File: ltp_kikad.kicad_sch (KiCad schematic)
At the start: 27 parts, among them IC1 SamacSys_Parts_HT16K33-28SOP, IC2 SamacSys_Parts_HT16K33-28SOP, J2 RPi_GPIO, J3 SM04B-SRSS-TB(LF)(SN)

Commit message: Minor fixes
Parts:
- added C11 (x2): 10uF, Capacitor_SMD:C_0603_1608Metric, symbol Device:C_Small
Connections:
- net +5V: now also C11.1, C11.1
- net GND: now also C11.2, C11.2
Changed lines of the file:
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@@
+    (stroke (width 0) (type default))
+  )
+  (wire (pts (xy 194.31 64.77) (xy 194.31 72.39))
     (stroke (width 0) (type default))
   )
@@
   )
   (wire (pts (xy 166.37 60.96) (xy 171.45 60.96))
+    (stroke (width 0) (type default))
+  )
+  (wire (pts (xy 273.05 110.49) (xy 273.05 118.11))
     (stroke (width 0) (type default))
   )
@@
     )
   )
+  (symbol (lib_id "power:GND") (at 273.05 123.19 0) (unit 1)
+    (in_bom yes) (on_board yes) (dnp no)
+    (property "Reference" "#PWR038" (at 273.05 129.54 0)
+      (effects (font (size 1.27 1.27)) hide)
+    )
+    (property "Value" "GND" (at 273.177 127.5842 0)
+      (effects (font (size 1.27 1.27)))
+    )
+    (property "Footprint" "" (at 273.05 123.19 0)
+      (effects (font (size 1.27 1.27)) hide)
+    )
+    (property "Datasheet" "" (at 273.05 123.19 0)
+      (effects (font (size 1.27 1.27)) hide)
+    )
+    (pin "1")
+    (instances
+      (project "LTP305_ESP32_CLOCK"
+        (path "/c007e288-8439-49d9-bbdf-49724c34958c"
+          (reference "#PWR038") (unit 1)
+        )
+      )
+      (project "ltp_kikad"
+        (path "/eed35b77-cbf9-4596-9b17-2558f81058ba"
+          (reference "#PWR028") (unit 1)
+        )
+      )
+    )
+  )
   (symbol (lib_id "power:GND") (at 114.3 137.16 0) (unit 1)
     (in_bom yes) (on_board yes) (dnp no)
@@
         (path "/eed35b77-cbf9-4596-9b17-2558f81058ba"
           (reference "#PWR012") (unit 1)
+        )
+      )
+    )
+  )
+  (symbol (lib_id "Device:C_Small") (at 273.05 120.65 0) (unit 1)
+    (in_bom yes) (on_board yes) (dnp no)
+    (property "Reference" "C11" (at 275.3868 119.4816 0)
+      (effects (font (size 1.27 1.27)) (justify left))
+    )
+    (property "Value" "10uF" (at 267.97 123.19 0)
+      (effects (font (size 1.27 1.27)) (justify left))
+    )
+    (property "Footprint" "Capacitor_SMD:C_0603_1608Metric" (at 273.05 120.65 0)
+      (effects (font (size 1.27 1.27)) hide)
+    )
+    (property "Datasheet" "~" (at 273.05 120.65 0)
+      (effects (font (size 1.27 1.27)) hide)
+    )
+    (pin "1")
+    (pin "2")
+    (instances
+      (project "LTP305_ESP32_CLOCK"
+        (path "/c007e288-8439-49d9-bbdf-49724c34958c"
+          (reference "C11") (unit 1)
+        )
+      )
+      (project "ltp_kikad"
+        (path "/eed35b77-cbf9-4596-9b17-2558f81058ba"
+          (reference "C14") (unit 1)
         )
       )
@@
         (path "/eed35b77-cbf9-4596-9b17-2558f81058ba"
           (reference "DS4") (unit 1)
+        )
+      )
+    )
+  )
+  (symbol (lib_id "power:+5V") (at 273.05 110.49 270) (unit 1)
+    (in_bom yes) (on_board yes) (dnp no)
+    (property "Reference" "#PWR08" (at 269.24 110.49 0)
+      (effects (font (size 1.27 1.27)) hide)
+    )
+    (property "Value" "+5V" (at 277.4442 110.871 0)
+      (effects (font (size 1.27 1.27)))
+    )
+    (property "Footprint" "" (at 273.05 110.49 0)
+      (effects (font (size 1.27 1.27)) hide)
+    )
+    (property "Datasheet" "" (at 273.05 110.49 0)
+      (effects (font (size 1.27 1.27)) hide)
+    )
+    (pin "1")
+    (instances
+      (project "LTP305_ESP32_CLOCK"
+        (path "/c007e288-8439-49d9-bbdf-49724c34958c"
+          (reference "#PWR08") (unit 1)
+        )
+      )
+      (project "ltp_kikad"
+        (path "/eed35b77-cbf9-4596-9b17-2558f81058ba"
+          (reference "#PWR027") (unit 1)
+        )
+      )
+    )
+  )
+  (symbol (lib_id "Device:C_Small") (at 194.31 74.93 0) (unit 1)
+    (in_bom yes) (on_board yes) (dnp no)
+    (property "Reference" "C11" (at 196.6468 73.7616 0)
+      (effects (font (size 1.27 1.27)) (justify left))
+    )
+    (property "Value" "10uF" (at 189.23 77.47 0)
+      (effects (font (size 1.27 1.27)) (justify left))
+    )
+    (property "Footprint" "Capacitor_SMD:C_0603_1608Metric" (at 194.31 74.93 0)
+      (effects (font (size 1.27 1.27)) hide)
+    )
+    (property "Datasheet" "~" (at 194.31 74.93 0)
+      (effects (font (size 1.27 1.27)) hide)
+    )
+    (pin "1")
+    (pin "2")
+    (instances
+      (project "LTP305_ESP32_CLOCK"
+        (path "/c007e288-8439-49d9-bbdf-49724c34958c"
+          (reference "C11") (unit 1)
+        )
+      )
+      (project "ltp_kikad"
+        (path "/eed35b77-cbf9-4596-9b17-2558f81058ba"
+          (reference "C15") (unit 1)
         )
       )
@@
     )
   )
+  (symbol (lib_id "power:+5V") (at 194.31 64.77 270) (unit 1)
+    (in_bom yes) (on_board yes) (dnp no)
+    (property "Reference" "#PWR08" (at 190.5 64.77 0)
+      (effects (font (size 1.27 1.27)) hide)
+    )
+    (property "Value" "+5V" (at 198.7042 65.151 0)
+      (effects (font (size 1.27 1.27)))
+    )
+    (property "Footprint" "" (at 194.31 64.77 0)
+      (effects (font (size 1.27 1.27)) hide)
+    )
+    (property "Datasheet" "" (at 194.31 64.77 0)
+      (effects (font (size 1.27 1.27)) hide)
+    )
+    (pin "1")
+    (instances
+      (project "LTP305_ESP32_CLOCK"
+        (path "/c007e288-8439-49d9-bbdf-49724c34958c"
+          (reference "#PWR08") (unit 1)
+        )
+      )
+      (project "ltp_kikad"
+        (path "/eed35b77-cbf9-4596-9b17-2558f81058ba"
+          (reference "#PWR029") (unit 1)
+        )
+      )
+    )
+  )
   (symbol (lib_id "power:GND") (at 255.27 158.75 0) (unit 1)
     (in_bom yes) (on_board yes) (dnp no)
@@
         )
       )
+    )
+  )
+  (symbol (lib_id "power:GND") (at 194.31 77.47 0) (unit 1)
+    (in_bom yes) (on_board yes) (dnp no)
+    (property "Reference" "#PWR038" (at 194.31 83.82 0)
+      (effects (font (size 1.27 1.27)) hide)
+    )
+    (property "Value" "GND" (at 194.437 81.8642 0)
+      (effects (font (size 1.27 1.27)))
+    )
+    (property "Footprint" "" (at 194.31 77.47 0)
+      (effects (font (size 1.27 1.27)) hide)
+    )
+    (property "Datasheet" "" (at 194.31 77.47 0)
+      (effects (font (size 1.27 1.27)) hide)
+    )
+    (pin "1")
+    (instances
+      (project "LTP305_ESP32_CLOCK"
+        (path "/c007e288-8439-49d9-bbdf-49724c34958c"
+          (reference "#PWR038") (unit 1)
+        )
+      )
+      (project "ltp_kikad"
+        (path "/eed35b77-cbf9-4596-9b17-2558f81058ba"
+          (reference "#PWR030") (unit 1)
+        )
+      )

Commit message: Miscellaneous optimisation
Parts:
- added C11 (x3): 10uF, Capacitor_SMD:C_0603_1608Metric, symbol Device:C_Small
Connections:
- net +5V: now also C11.1, C11.1, C11.1
- net GND: now also C11.2, C11.2, C11.2

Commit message: Updates to 0.03
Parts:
- added R3, R5: DNP, Resistor_SMD:R_0603_1608Metric_Pad0.98x0.95mm_HandSolder, symbol Device:R
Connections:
- net +5V: now also R3.1, R5.1
- net SCL: now also R5.2
- net SDA: now also R3.2
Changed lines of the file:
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@@
   (junction (at 242.57 152.4) (diameter 1.016) (color 0 0 0 0)
   )
+  (junction (at 254 20.32) (diameter 0) (color 0 0 0 0)
+  )
   (junction (at 195.58 129.54) (diameter 0) (color 0 0 0 0)
   )
@@
     (stroke (width 0) (type default))
   )
-  (wire (pts (xy 217.17 152.4) (xy 242.57 152.4))
+  (wire (pts (xy 224.79 152.4) (xy 242.57 152.4))
     (stroke (width 0) (type solid))
   )
@@
     (stroke (width 0) (type default))
   )
-  (wire (pts (xy 217.17 149.86) (xy 233.68 149.86))
+  (wire (pts (xy 224.79 149.86) (xy 233.68 149.86))
     (stroke (width 0) (type solid))
   )
@@
     (stroke (width 0) (type default))
   )
+  (wire (pts (xy 247.65 29.21) (xy 247.65 26.67))
+    (stroke (width 0) (type default))
+  )
   (wire (pts (xy 166.37 81.28) (xy 171.45 81.28))
     (stroke (width 0) (type default))
@@
     (stroke (width 0) (type default))
   )
+  (wire (pts (xy 254 21.59) (xy 254 20.32))
+    (stroke (width 0) (type default))
+  )
   (wire (pts (xy 251.46 109.22) (xy 251.46 116.84))
     (stroke (width 0) (type default))
@@
     (stroke (width 0) (type default))
   )
+  (wire (pts (xy 231.14 30.48) (xy 259.08 30.48))
+    (stroke (width 0) (type default))
+  )
   (wire (pts (xy 157.48 166.37) (xy 160.02 166.37))
     (stroke (width 0) (type default))
@@
     (stroke (width 0) (type default))
   )
+  (wire (pts (xy 231.14 26.67) (xy 247.65 26.67))
+    (stroke (width 0) (type default))
+  )
   (wire (pts (xy 114.3 134.62) (xy 114.3 137.16))
     (stroke (width 0) (type default))
@@
     (stroke (width 0) (type default))
   )
+  (wire (pts (xy 247.65 29.21) (xy 250.19 29.21))
+    (stroke (width 0) (type default))
+  )
   (wire (pts (xy 227.33 118.11) (xy 212.09 118.11))
     (stroke (width 0) (type default))
@@
     (stroke (width 0) (type default))
   )
+  (wire (pts (xy 250.19 21.59) (xy 254 21.59))
+    (stroke (width 0) (type default))
+  )
   (wire (pts (xy 252.73 144.78) (xy 260.35 144.78))
     (stroke (width 0) (type solid))
@@
     (stroke (width 0) (type default))
   )
+  (wire (pts (xy 259.08 20.32) (xy 259.08 22.86))
+    (stroke (width 0) (type default))
+  )
   (wire (pts (xy 119.38 118.11) (xy 119.38 114.3))
     (stroke (width 0) (type default))
@@
     (stroke (width 0) (type default))
   )
+  (wire (pts (xy 254 20.32) (xy 259.08 20.32))
+    (stroke (width 0) (type default))
+  )
   (wire (pts (xy 205.74 64.77) (xy 205.74 72.39))
     (stroke (width 0) (type default))
@@
     )
   )
+  (global_label "SCL" (shape input) (at 231.14 30.48 180)
+    (effects (font (size 1.27 1.27)) (justify right))
+    (property "Intersheetrefs" "${INTERSHEET_REFS}" (at 224.7266 30.48 0)
+      (effects (font (size 1.27 1.27)) hide)
+    )
+  )
   (global_label "2_ca3" (shape input) (at 25.4 125.73 180)
     (effects (font (size 1.27 1.27)) (justify right))
@@
     )
   )
-  (global_label "SCL" (shape input) (at 217.17 152.4 180)
+  (global_label "SCL" (shape input) (at 224.79 152.4 180)
     (effects (font (size 1.27 1.27)) (justify right))
-    (property "Intersheetrefs" "${INTERSHEET_REFS}" (at 210.7566 152.4 0)
+    (property "Intersheetrefs" "${INTERSHEET_REFS}" (at 218.3766 152.4 0)
       (effects (font (size 1.27 1.27)) hide)
     )
@@
     )
   )
+  (global_label "SDA" (shape input) (at 231.14 26.67 180)
+    (effects (font (size 1.27 1.27)) (justify right))
+    (property "Intersheetrefs" "${INTERSHEET_REFS}" (at 231.14 26.67 0)
+      (effects (font (size 1.27 1.27)) hide)
+    )
+  )
   (global_label "2_an9" (shape input) (at 24.13 153.67 180)
     (effects (font (size 1.27 1.27)) (justify right))
@@
     )
   )
-  (global_label "SDA" (shape input) (at 217.17 149.86 180)
+  (global_label "SDA" (shape input) (at 224.79 149.86 180)
     (effects (font (size 1.27 1.27)) (justify right))
-    (property "Intersheetrefs" "${INTERSHEET_REFS}" (at 217.17 149.86 0)
+    (property "Intersheetrefs" "${INTERSHEET_REFS}" (at 224.79 149.86 0)
       (effects (font (size 1.27 1.27)) hide)
     )
@@
     )
   )
+  (symbol (lib_id "Device:R") (at 250.19 25.4 0) (unit 1)
+    (in_bom yes) (on_board yes) (dnp no)
+    (property "Reference" "R3" (at 252.73 24.13 0)
+      (effects (font (size 1.27 1.27)) (justify left))
+    )
+    (property "Value" "DNP" (at 252.73 25.4 0)
+      (effects (font (size 1.27 1.27)) (justify left))
+    )
+    (property "Footprint" "Resistor_SMD:R_0603_1608Metric_Pad0.98x0.95mm_HandSolder" (at 248.412 25.4 90)
+      (effects (font (size 1.27 1.27)) hide)
+    )
+    (property "Datasheet" "~" (at 250.19 25.4 0)
+      (effects (font (size 1.27 1.27)) hide)
+    )
+    (pin "1")
+    (pin "2")
+    (instances
+      (project "cm4-gpio"
+        (path "/9052c69d-def3-4232-bac1-59988fb85f45"
+          (reference "R3") (unit 1)
+        )
+      )
+      (project "ltp_kikad"
+        (path "/eed35b77-cbf9-4596-9b17-2558f81058ba"
+          (reference "R4") (unit 1)
+        )
+      )
+    )
+  )
   (symbol (lib_id "power:+5V") (at 261.62 111.76 270) (unit 1)
     (in_bom yes) (on_board yes) (dnp no)
@@
     )
   )
+  (symbol (lib_id "power:+5V") (at 254 20.32 0) (unit 1)
+    (in_bom yes) (on_board yes) (dnp no)
+    (property "Reference" "#PWR08" (at 254 24.13 0)
+      (effects (font (size 1.27 1.27)) hide)
+    )
+    (property "Value" "+5V" (at 254.381 15.9258 0)
+      (effects (font (size 1.27 1.27)))
+    )
+    (property "Footprint" "" (at 254 20.32 0)
+      (effects (font (size 1.27 1.27)) hide)
+    )
+    (property "Datasheet" "" (at 254 20.32 0)
+      (effects (font (size 1.27 1.27)) hide)
+    )
+    (pin "1")
+    (instances
+      (project "LTP305_ESP32_CLOCK"
+        (path "/c007e288-8439-49d9-bbdf-49724c34958c"
+          (reference "#PWR08") (unit 1)
+        )
+      )
+      (project "ltp_kikad"
+        (path "/eed35b77-cbf9-4596-9b17-2558f81058ba"
+          (reference "#PWR037") (unit 1)
+        )
+      )
+    )
+  )
   (symbol (lib_id "LTP-305G:LTP-305G") (at 30.48 118.11 0) (unit 1)
     (in_bom yes) (on_board yes) (dnp no) (fields_autoplaced)
@@
         )
       )
+    )
+  )
+  (symbol (lib_id "Device:R") (at 259.08 26.67 0) (unit 1)
+    (in_bom yes) (on_board yes) (dnp no)
+    (property "Reference" "R5" (at 261.62 25.4 0)
+      (effects (font (size 1.27 1.27)) (justify left))
+    )
+    (property "Value" "DNP" (at 261.62 26.67 0)
+      (effects (font (size 1.27 1.27)) (justify left))
+    )
+    (property "Footprint" "Resistor_SMD:R_0603_1608Metric_Pad0.98x0.95mm_HandSolder" (at 257.302 26.67 90)
+      (effects (font (size 1.27 1.27)) hide)
+    )
+    (property "Datasheet" "~" (at 259.08 26.67 0)
+      (effects (font (size 1.27 1.27)) hide)
+    )
+    (pin "1")
+    (pin "2")
+    (instances
+      (project "cm4-gpio"
+        (path "/9052c69d-def3-4232-bac1-59988fb85f45"
+          (reference "R5") (unit 1)
+        )
+      )
+      (project "ltp_kikad"
+        (path "/eed35b77-cbf9-4596-9b17-2558f81058ba"
+          (reference "R5") (unit 1)
+        )
+      )

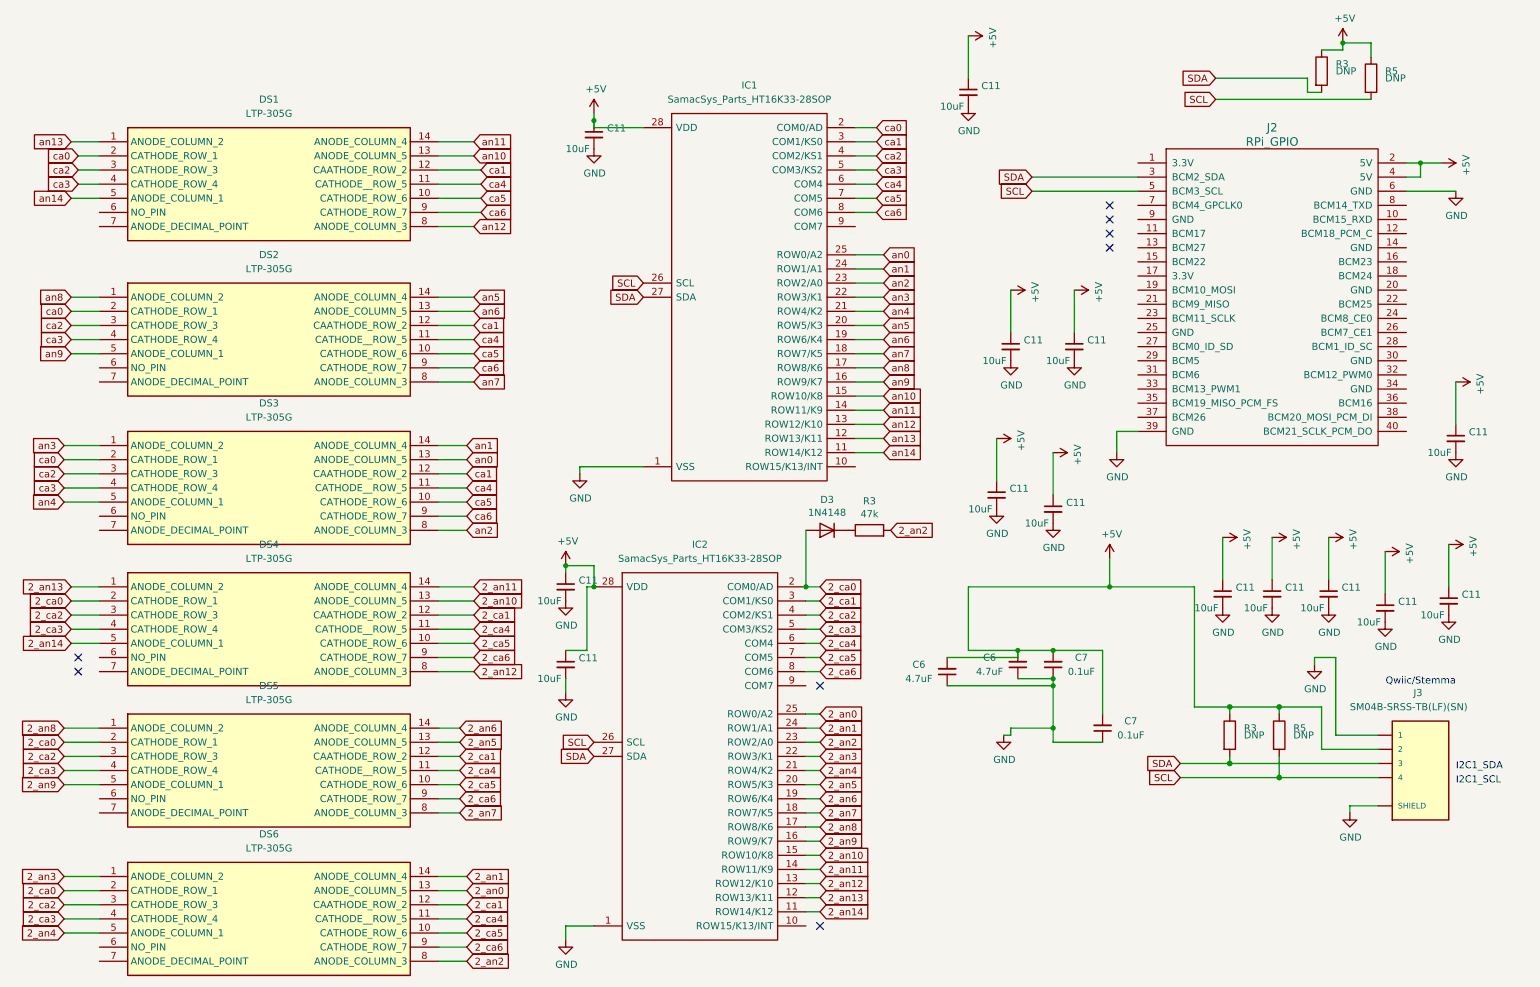
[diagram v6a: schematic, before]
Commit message: V 0.04a 0Add CAN tranciver, set 3d models for components
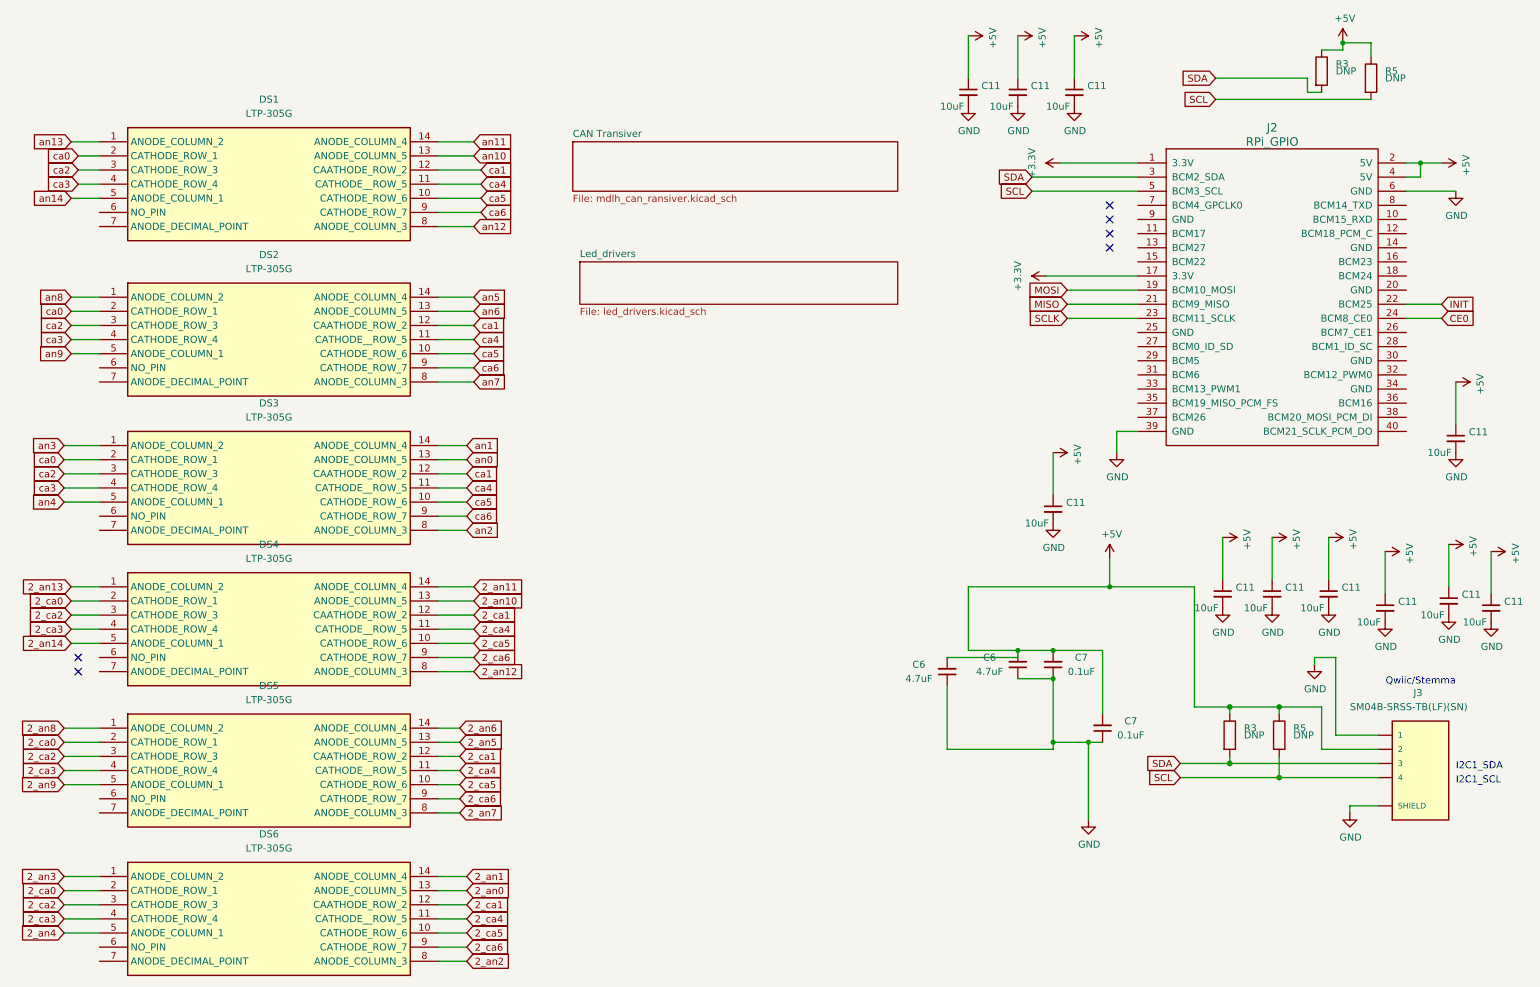
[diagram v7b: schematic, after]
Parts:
- removed C11 (x3): 10uF, Capacitor_SMD:C_0603_1608Metric, symbol Device:C_Small
- removed D3: 1N4148, Diode_SMD:D_SOD-123, symbol Device:D
- removed IC1, IC2: SamacSys_Parts_HT16K33-28SOP, Holtek:SOIC127P1031X264-28N, symbol LTP305_ESP32_CLOCK-rescue:HT16K33-28SOP-SamacSys_Parts
- removed R3: 47k, Resistor_SMD:R_0603_1608Metric, symbol Device:R
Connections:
- net +3.3V: now reaches J2.1 (3.3V)
- net +3.3V: now also J2.17 (3.3V)
- net MOSI: now reaches J2.19 (BCM10_MOSI)
- net MISO: now reaches J2.21 (BCM9_MISO)
- net INIT: now reaches J2.22 (BCM25)
- net SCLK: now reaches J2.23 (BCM11_SCLK)
- net CE0: now reaches J2.24 (BCM8_CE0)
- no-connect marks 8 -> 6
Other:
- added sheet CAN Transiver (mdlh_can_ransiver.kicad_sch)
- added sheet Led_drivers (led_drivers.kicad_sch)
- moved on the sheet: C11
